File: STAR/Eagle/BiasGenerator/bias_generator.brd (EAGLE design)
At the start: 54.6 x 29.8 mm, 24 parts, among them J1 J30J-9J30, T1 750311838, U1 LT8300, U2 LT8330

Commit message: misc board stuff
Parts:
- C4: value 1uF -> 10uF; device AR_passives:0603 -> AR_passives:2J-LEAD
- C7: value 10uF -> 1uF; device AR_passives:2J-LEAD -> AR_passives:0603
- D1: value BAV20W -> MMSZ5266BT1G; device AR_diode:SOD323 -> AR_diode:SOD123
- D2: value MMSZ5266BT1G -> BAV20W; device AR_diode:SOD123 -> AR_diode:SOD323
- R1: value 407k -> 47k; device resistor:R0603 -> resistor:R2512
- R2: value 1k -> 407k
- R3: value 1M -> 1k
- R4: value 1M -> 3k; device resistor:R0603 -> resistor:R2512
- R5: value 1M -> 1.5k; device resistor:R0603 -> resistor:R2512
- R6: value 1.5k -> 1M; device resistor:R2512 -> resistor:R0603
- R7: value 47k -> 1M; device resistor:R2512 -> resistor:R0603
- R8: value 3k -> 1M; device resistor:R2512 -> resistor:R0603
- moved C7 32.6 mm to (31.8, 2.54), turned to 0 degrees
- moved R6 25.8 mm to (24.1, 9.84), turned to 0 degrees
- moved R5 24.5 mm to (3.81, 25.7), turned to 270 degrees
- moved C4 17.8 mm to (8.89, 25.7), turned to 90 degrees
- moved C5 15.9 mm to (24.1, 16.5), turned to 180 degrees
- moved R1 15.4 mm to (18.7, 5.71), turned to 90 degrees
- moved R3 13.1 mm to (14.0, 18.1), turned to 180 degrees
- moved R4 12.8 mm to (14.6, 5.71), turned to 90 degrees
- moved R8 11.4 mm to (24.1, 12.1), turned to 0 degrees
- moved R7 10.1 mm to (24.1, 14.3), turned to 180 degrees
- moved D1 2.42 mm to (9.84, 18.1), turned to 0 degrees
- moved D2 2.42 mm to (10.8, 20.3), turned to 180 degrees
- moved R2 2.22 mm to (14.0, 20.3), turned to 0 degrees
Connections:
- net +20V: now also C5.1; no longer C4.1
- net +50V: now also C4.P$1, R1.2, R5.2; no longer C7.P$1, R3.2, R7.2
- net GND: now also C4.P$2, C7.2, R4.1; no longer C4.2, C7.P$2, R6.1
- net N$11: now also R7.1, R8.2; no longer R4.1, R5.2
- net N$2: now also R2.1; no longer R1.1
- net N$3: now also R2.2, R3.1; no longer R1.2, R2.1
- net N$4: now also D2.P$1, R3.2; no longer D1.P$1, R2.2
- net N$6: now also C7.1; no longer C5.1
- net N$9: now also R6.1, R7.2; no longer R3.1, R4.2
- net VCC: now also D1.P$1; no longer D2.P$1
- net V_DIVIDE: now also R1.1, R4.2; no longer R7.1, R8.2
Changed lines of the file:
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@@
 <attribute name="VALUE" x="27.6225" y="2.8575" size="1.27" layer="27"/>
 </element>
-<element name="C4" library="AR_passives" package="0603" value="1uF" x="24.13" y="16.51" smashed="yes" rot="R180">
+<element name="C5" library="AR_passives" package="0603" value="1uF" x="24.13" y="16.51" smashed="yes" rot="R180">
 <attribute name="NAME" x="27.686" y="17.018" size="1.016" layer="25" font="vector" rot="R180"/>
 <attribute name="VALUE" x="24.765" y="18.923" size="1.27" layer="27" rot="R180"/>
 </element>
-<element name="C5" library="AR_passives" package="0603" value="1uF" x="31.75" y="2.54" smashed="yes">
+<element name="C7" library="AR_passives" package="0603" value="1uF" x="31.75" y="2.54" smashed="yes">
 <attribute name="NAME" x="35.433" y="2.9845" size="1.016" layer="25" font="vector" rot="R180"/>
 <attribute name="VALUE" x="31.115" y="0.127" size="1.27" layer="27"/>
@@
 <attribute name="VALUE" x="6.985" y="17.907" size="1.27" layer="27"/>
 </element>
-<element name="C7" library="AR_passives" package="2J-LEAD" value="10uF" x="8.89" y="25.7175" smashed="yes" rot="R90">
+<element name="C4" library="AR_passives" package="2J-LEAD" value="10uF" x="8.89" y="25.7175" smashed="yes" rot="R90">
 <attribute name="NAME" x="5.89" y="23.7175" size="1.27" layer="27" rot="R90"/>
 <attribute name="VALUE" x="13.89" y="23.7175" size="1.27" layer="27" rot="R90"/>
 </element>
-<element name="D1" library="AR_diode" package="SOD323" value="BAV20W" x="10.795" y="20.32" smashed="yes" rot="R180">
+<element name="D2" library="AR_diode" package="SOD323" value="BAV20W" x="10.795" y="20.32" smashed="yes" rot="R180">
 <attribute name="NAME" x="10.2855" y="21.143" size="1.016" layer="25" font="vector"/>
 <attribute name="VALUE" x="11.595" y="21.77" size="0.6096" layer="27" rot="R180"/>
 </element>
-<element name="D2" library="AR_diode" package="SOD123" value="MMSZ5266BT1G" x="9.8425" y="18.0975" smashed="yes">
+<element name="D1" library="AR_diode" package="SOD123" value="MMSZ5266BT1G" x="9.8425" y="18.0975" smashed="yes">
 <attribute name="NAME" x="10.2805" y="17.1575" size="1.016" layer="25" font="vector" rot="R270"/>
 <attribute name="VALUE" x="8.2425" y="16.1975" size="0.8128" layer="27"/>
@@
 </element>
 <element name="L1" library="AR_passives" package="PQ2614" value="10uH" x="43.815" y="15.875" smashed="yes" rot="R270"/>
-<element name="R1" library="resistor" package="R0603" value="407k" x="13.97" y="20.32" smashed="yes">
+<element name="R2" library="resistor" package="R0603" value="407k" x="13.97" y="20.32" smashed="yes">
 <attribute name="NAME" x="16.4465" y="19.431" size="1.016" layer="25" font="vector" rot="R90"/>
 <attribute name="VALUE" x="13.335" y="18.415" size="1.27" layer="27"/>
 </element>
-<element name="R2" library="resistor" package="R0603" value="1k" x="13.97" y="18.0975" smashed="yes" rot="R180">
+<element name="R3" library="resistor" package="R0603" value="1k" x="13.97" y="18.0975" smashed="yes" rot="R180">
 <attribute name="NAME" x="15.621" y="18.4785" size="1.016" layer="25" font="vector" rot="R270"/>
 <attribute name="VALUE" x="14.605" y="20.0025" size="1.27" layer="27" rot="R180"/>
 </element>
-<element name="R3" library="resistor" package="R0603" value="1M" x="24.13" y="9.8425" smashed="yes">
+<element name="R6" library="resistor" package="R0603" value="1M" x="24.13" y="9.8425" smashed="yes">
 <attribute name="NAME" x="20.955" y="9.017" size="1.016" layer="25" font="vector"/>
 <attribute name="VALUE" x="23.495" y="7.9375" size="1.27" layer="27"/>
 </element>
-<element name="R4" library="resistor" package="R0603" value="1M" x="24.13" y="14.2875" smashed="yes" rot="R180">
+<element name="R7" library="resistor" package="R0603" value="1M" x="24.13" y="14.2875" smashed="yes" rot="R180">
 <attribute name="NAME" x="27.559" y="14.6685" size="1.016" layer="25" font="vector" rot="R180"/>
 <attribute name="VALUE" x="24.765" y="16.1925" size="1.27" layer="27" rot="R180"/>
 </element>
-<element name="R5" library="resistor" package="R0603" value="1M" x="24.13" y="12.065" smashed="yes">
+<element name="R8" library="resistor" package="R0603" value="1M" x="24.13" y="12.065" smashed="yes">
 <attribute name="NAME" x="22.479" y="11.3665" size="1.016" layer="25" font="vector" rot="R90"/>
 <attribute name="VALUE" x="23.495" y="10.16" size="1.27" layer="27"/>
 </element>
-<element name="R6" library="resistor" package="R2512" value="1.5k" x="3.81" y="25.7175" smashed="yes" rot="R270">
+<element name="R5" library="resistor" package="R2512" value="1.5k" x="3.81" y="25.7175" smashed="yes" rot="R270">
 <attribute name="NAME" x="2.9845" y="25.146" size="1.016" layer="25" font="vector"/>
 <attribute name="VALUE" x="0.635" y="28.2575" size="1.27" layer="27" rot="R270"/>
@@
 </element>
 <element name="U2" library="AR_IC" package="8-DFN" value="LT8330" x="27.432" y="2.54" smashed="yes" rot="R270"/>
-<element name="R7" library="resistor" package="R2512" value="47k" x="18.7325" y="5.715" smashed="yes" rot="R90">
+<element name="R1" library="resistor" package="R2512" value="47k" x="18.7325" y="5.715" smashed="yes" rot="R90">
 <attribute name="NAME" x="19.812" y="5.842" size="1.016" layer="25" font="vector" rot="R180"/>
 <attribute name="VALUE" x="21.9075" y="3.175" size="1.27" layer="27" rot="R90"/>
 </element>
-<element name="R8" library="resistor" package="R2512" value="3k" x="14.605" y="5.715" smashed="yes" rot="R90">
+<element name="R4" library="resistor" package="R2512" value="3k" x="14.605" y="5.715" smashed="yes" rot="R90">
 <attribute name="NAME" x="15.494" y="6.096" size="1.016" layer="25" font="vector" rot="R180"/>
 <attribute name="VALUE" x="17.78" y="3.175" size="1.27" layer="27" rot="R90"/>
@@
 <contactref element="U1" pad="5"/>
 <contactref element="C2" pad="1"/>
-<contactref element="D2" pad="P$1"/>
+<contactref element="D1" pad="P$1"/>
 <contactref element="T1" pad="P$3"/>
 <contactref element="C1" pad="P$1"/>
@@
 <contactref element="T1" pad="P$7"/>
 <contactref element="C3" pad="2"/>
-<contactref element="C4" pad="2"/>
 <contactref element="C5" pad="2"/>
+<contactref element="C7" pad="2"/>
 <contactref element="U2" pad="P$5"/>
 <contactref element="U2" pad="P$9"/>
+<contactref element="R8" pad="1"/>
+<contactref element="C4" pad="P$2"/>
 <contactref element="R5" pad="1"/>
-<contactref element="C7" pad="P$2"/>
-<contactref element="R6" pad="1"/>
-<contactref element="R8" pad="1"/>
+<contactref element="R4" pad="1"/>
 <contactref element="J1" pad="7"/>
 <polygon width="0.4064" layer="1" rank="6">
@@
 </signal>
 <signal name="N$1">
+<contactref element="D1" pad="P$2"/>
 <contactref element="D2" pad="P$2"/>
-<contactref element="D1" pad="P$2"/>
 <wire x1="11.4175" y1="18.0975" x2="11.4175" y2="18.6475" width="0.4064" layer="1"/>
 <wire x1="11.4175" y1="18.6475" x2="9.745" y2="20.32" width="0.4064" layer="1"/>
@@
 <signal name="N$4">
 <contactref element="U1" pad="4"/>
-<contactref element="D1" pad="P$1"/>
-<contactref element="R2" pad="2"/>
+<contactref element="D2" pad="P$1"/>
+<contactref element="R3" pad="2"/>
 <contactref element="T1" pad="P$4"/>
 <wire x1="11.845" y1="20.32" x2="11.845" y2="19.3725" width="0.4572" layer="1"/>
@@
 <contactref element="D3" pad="P$2"/>
 <contactref element="C3" pad="1"/>
-<contactref element="C4" pad="1"/>
+<contactref element="C5" pad="1"/>
 <contactref element="L1" pad="P$2"/>
 <contactref element="U2" pad="P$6"/>
@@
 </signal>
 <signal name="N$6">
-<contactref element="C5" pad="1"/>
+<contactref element="C7" pad="1"/>
 <contactref element="U2" pad="P$7"/>
 <wire x1="28.357" y1="2.79" x2="29.2695" y2="2.79" width="0.2032" layer="1"/>
@@
 <contactref element="U2" pad="P$1"/>
 <contactref element="C6" pad="2"/>
-<contactref element="R3" pad="1"/>
-<contactref element="R4" pad="2"/>
+<contactref element="R6" pad="1"/>
+<contactref element="R7" pad="2"/>
 <via x="10.287" y="18.034" extent="1-16" drill="0.6"/>
 <wire x1="10.287" y1="18.034" x2="20.7645" y2="18.034" width="0.4064" layer="16"/>
@@
 <signal name="N$2">
 <contactref element="U1" pad="3"/>
-<contactref element="R1" pad="1"/>
+<contactref element="R2" pad="1"/>
 <wire x1="14.5415" y1="21.2725" x2="14.92" y2="21.651" width="0.4064" layer="1"/>
 <wire x1="14.92" y1="21.651" x2="14.92" y2="22.5065" width="0.4064" layer="1"/>
@@
 </signal>
 <signal name="N$3">
-<contactref element="R2" pad="1"/>
-<contactref element="R1" pad="2"/>
+<contactref element="R3" pad="1"/>
+<contactref element="R2" pad="2"/>
 <wire x1="14.82" y1="18.0975" x2="14.82" y2="20.32" width="0.4064" layer="1"/>
 </signal>
 <signal name="+50V">
 <contactref element="C6" pad="1"/>
-<contactref element="R3" pad="2"/>
+<contactref element="R6" pad="2"/>
 <contactref element="D4" pad="P$2"/>
-<contactref element="C7" pad="P$1"/>
-<contactref element="R6" pad="2"/>
-<contactref element="R7" pad="2"/>
+<contactref element="C4" pad="P$1"/>
+<contactref element="R5" pad="2"/>
+<contactref element="R1" pad="2"/>
 <wire x1="3.81" y1="22.9175" x2="8.382" y2="22.9175" width="0.4064" layer="1"/>
 <wire x1="8.382" y1="22.9175" x2="8.74" y2="22.9175" width="0.4064" layer="1"/>
@@
 </signal>
 <signal name="N$11">
-<contactref element="R4" pad="1"/>
-<contactref element="R5" pad="2"/>
+<contactref element="R7" pad="1"/>
+<contactref element="R8" pad="2"/>
 <wire x1="24.98" y1="14.2875" x2="24.98" y2="12.065" width="0.4064" layer="1"/>
 </signal>
 <signal name="V_DIVIDE">
 <contactref element="J1" pad="5"/>
-<contactref element="R7" pad="1"/>
-<contactref element="R8" pad="2"/>
+<contactref element="R1" pad="1"/>
+<contactref element="R4" pad="2"/>
 <wire x1="18.7325" y1="2.915" x2="18.421" y2="2.915" width="0.4064" layer="1"/>
 <wire x1="18.421" y1="2.915" x2="16.7005" y2="4.6355" width="0.4064" layer="1"/>

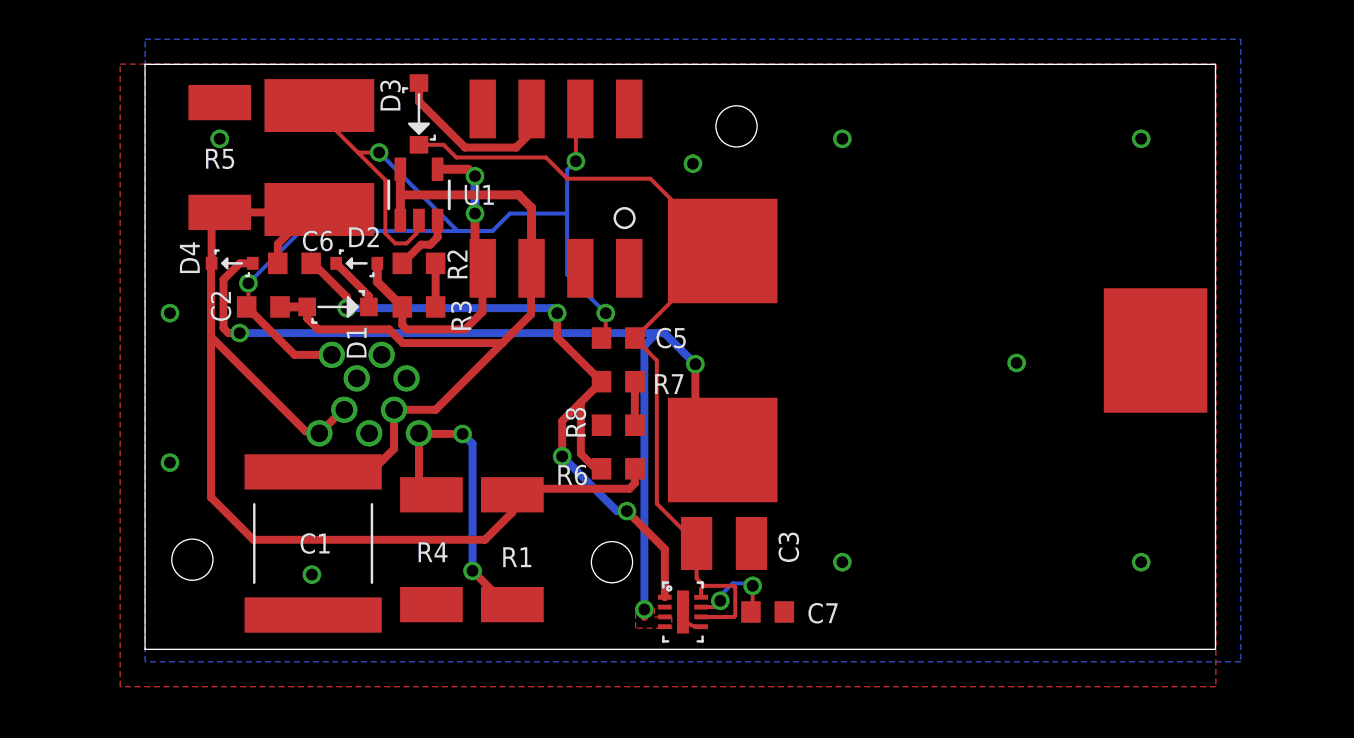
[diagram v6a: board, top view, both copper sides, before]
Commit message: updated bias board cad
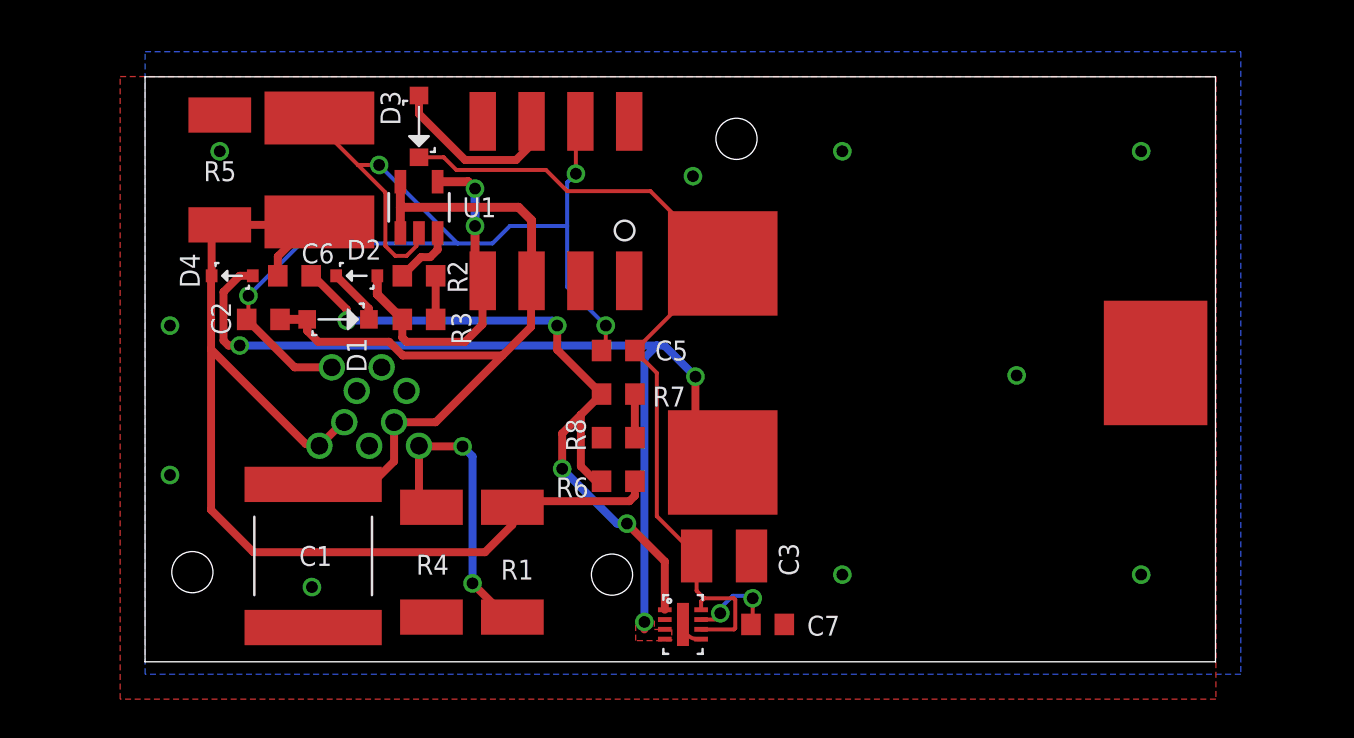
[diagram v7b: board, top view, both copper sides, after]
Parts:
- moved C2 0.64 mm to (6.03, 17.5)
- moved C4 0.64 mm to (8.89, 25.1)
- moved C5 0.64 mm to (24.1, 15.9)
- moved C6 0.64 mm to (7.62, 19.7)
- moved D1 0.64 mm to (9.84, 17.5)
- moved D2 0.64 mm to (10.8, 19.7)
- moved D3 0.64 mm to (14.0, 27.3)
- moved D4 0.64 mm to (4.45, 19.7)
- moved R2 0.64 mm to (14.0, 19.7)
- moved R3 0.64 mm to (14.0, 17.5)
- moved R5 0.64 mm to (3.81, 25.1)
- moved U1 0.64 mm to (14.0, 23.2)
- moved C7 0.64 mm to (31.8, 1.91)
- moved U2 0.64 mm to (27.4, 1.91)
- moved C1 0.63 mm to (8.57, 5.40)
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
